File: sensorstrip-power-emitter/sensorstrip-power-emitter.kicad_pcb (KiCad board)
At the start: 2 copper layers, 56 x 13 mm, 15 parts, among them J1 USB_C_Receptacle_PowerOnly, J2 Conn_01x02_MountingPin, SW1 SW_DPDT_x2

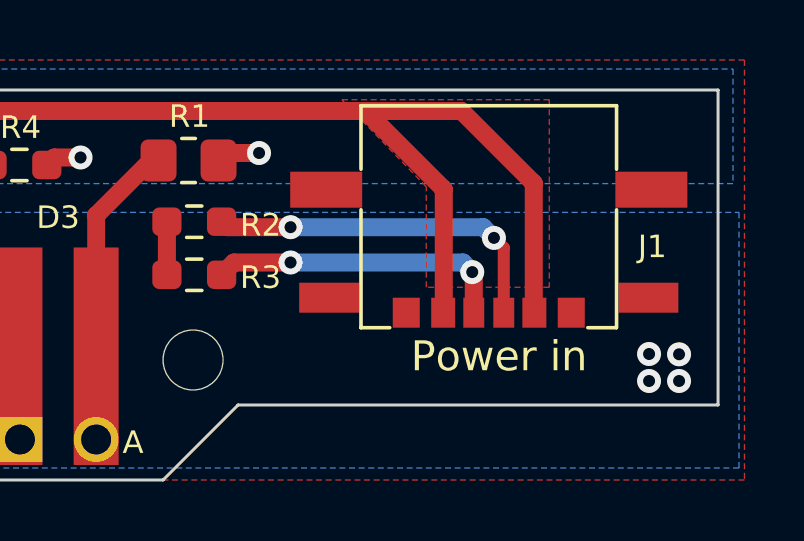
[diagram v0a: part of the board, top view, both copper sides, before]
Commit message: Update USB-C connector
Allowances for GCT USB4135-GF-A footprint
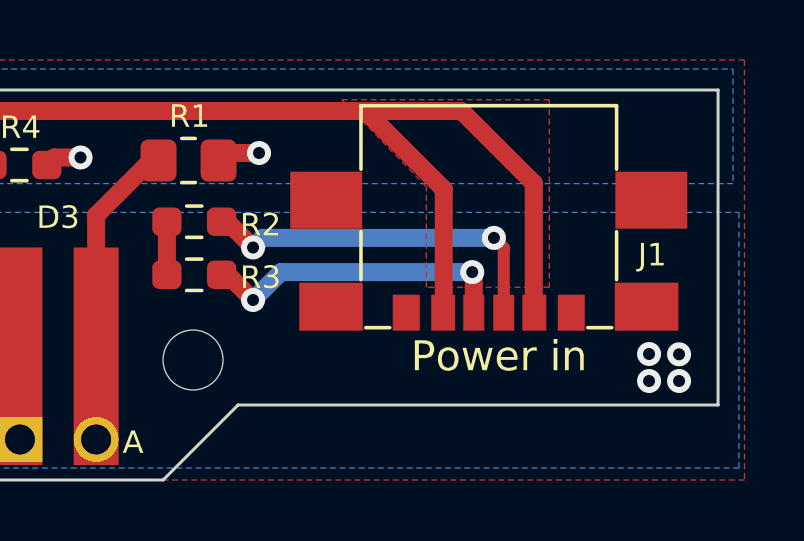
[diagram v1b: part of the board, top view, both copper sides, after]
